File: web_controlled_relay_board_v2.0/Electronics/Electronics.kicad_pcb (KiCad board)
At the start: 2 copper layers, 67 parts, among them J3 Screw_Terminal_01x02, J4 Screw_Terminal_01x02, K1 G3MB-202P, K10 G3MB-202P, K11 G3MB-202P, K12 G3MB-202P, K13 G3MB-202P, K14 G3MB-202P, K15 G3MB-202P, K16 G3MB-202P, K17 G3MB-202P, K18 G3MB-202P, K19 G3MB-202P, K2 G3MB-202P, K20 G3MB-202P, K3 G3MB-202P, K4 G3MB-202P, K5 G3MB-202P, K6 G3MB-202P, K7 G3MB-202P, K8 G3MB-202P, K9 G3MB-202P, SW1 SW_MEC_5E, U1 PC817, U10 PC817, U11 PC817, U12 PC817, U13 PC817, U14 PC817, U15 PC817, U16 PC817, U17 PC817, U18 PC817, U19 PC817, U2 PC817, U20 PC817, U3 PC817, U4 PC817, U5 PC817, U6 PC817, U7 PC817, U8 PC817, U9 PC817

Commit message: PCB finished, pending final touches
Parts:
- added J1: Screw_Terminal_01x10, TerminalBlock_CUI:TerminalBlock_CUI_TB007-508-10_1x10_P5.08mm_Horizontal, F.Cu at (187.8, 47.4)
- added J2: Screw_Terminal_01x10, TerminalBlock_CUI:TerminalBlock_CUI_TB007-508-10_1x10_P5.08mm_Horizontal, F.Cu at (187.8, 128.3)
- moved J3 156.8 mm to (188.0, 33.0), turned to -90 degrees
- moved K1 149.9 mm to (167.9, 31.8)
- moved K10 149.9 mm to (167.9, 106.4)
- moved K2 149.9 mm to (167.9, 40.1)
- moved K3 149.9 mm to (167.9, 48.4)
- moved K4 149.9 mm to (167.9, 56.7)
- moved K5 149.9 mm to (167.9, 65.0)
- moved K6 149.9 mm to (167.9, 73.3)
- moved K7 149.9 mm to (167.9, 81.6)
- moved K8 149.9 mm to (167.9, 89.8)
- moved K9 149.9 mm to (167.9, 98.1)
- moved A1 135.4 mm to (105.8, 190.6), turned to 180 degrees
- moved R17 135.1 mm to (112.4, 178.6)
- moved R19 135.1 mm to (112.4, 186.7)
- moved R15 135.1 mm to (112.4, 170.5)
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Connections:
- A1 pad 1: Control0 -> Control19
- A1 pad 10: Control7 -> Control12
- A1 pad 11: Control8 -> Control11
- A1 pad 12: Control9 -> Control10
- A1 pad 14: Control10 -> Control9
- A1 pad 15: Control11 -> Control8
- A1 pad 16: Control12 -> Control7
- A1 pad 17: Control13 -> Control6
- A1 pad 19: Control14 -> Control5
- A1 pad 2: Control1 -> Control18
- A1 pad 20: Control15 -> Control4
- A1 pad 21: Control16 -> Control3
- A1 pad 22: Control17 -> Control2
- A1 pad 24: Control18 -> Control1
- A1 pad 25: Control19 -> Control0
- A1 pad 39: unconnected-(A1-VSYS-Pad39) -> Net-(A1-VSYS)
- A1 pad 4: Control2 -> Control17
- A1 pad 5: Control3 -> Control16
- A1 pad 6: Control4 -> Control15
- A1 pad 7: Control5 -> Control14
- A1 pad 9: Control6 -> Control13
- J4 pad 1: NEUT -> AC
- J4 pad 2: AC -> NEUT
- PS2 pad 1: AC -> NEUT
- PS2 pad 2: NEUT -> AC
- PowerPin1 pad 2: unconnected-(PowerPin1-Pin_2-Pad2) -> Net-(A1-VSYS)
- U1 pad 1: Net-(R1-Pad2) -> Net-(R2-Pad2)
- U2 pad 1: Net-(R2-Pad2) -> Net-(R1-Pad2)
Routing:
- net GNDA: track 0.00 -> 305.9 mm
- net GND: track 0.00 -> 295.7 mm
- net +5V: track 0.00 -> 213.8 mm
- net GNDD: track 0.00 -> 183.1 mm
- net +3.3V: track 0.00 -> 102.2 mm
- net NEUT: track 0.00 -> 61.1 mm
- net AC: track 0.00 -> 57.3 mm
- net Net-(K1-Pad4): track 0.00 -> 56.7 mm
- net Control0: track 0.00 -> 55.0 mm
- net Net-(K2-Pad4): track 0.00 -> 54.0 mm
- net Net-(K3-Pad4): track 0.00 -> 51.3 mm
- net Net-(K4-Pad4): track 0.00 -> 48.6 mm
- net Control1: track 0.00 -> 48.3 mm
- net Net-(K5-Pad4): track 0.00 -> 46.0 mm
- net Net-(K6-Pad4): track 0.00 -> 43.3 mm
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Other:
- board outline added: 118.9 x 165.9 mm

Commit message: finished final touches of PCB schematic and layout
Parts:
- added C1: C_Polarized, Capacitor_THT:CP_Radial_D6.3mm_P2.50mm, F.Cu at (66.2, 81.6)
- added C2: C_Polarized, Capacitor_THT:CP_Radial_D8.0mm_P3.50mm, F.Cu at (86.7, 28.8)
- moved SW1 62.9 mm to (30.8, 117.9)
- moved U14 55.7 mm to (75.7, 147.3)
- moved U15 55.7 mm to (75.7, 152.9)
- moved U18 55.7 mm to (75.7, 169.7)
- moved J2 55.7 mm to (132.6, 120.9)
- moved J3 55.7 mm to (132.7, 25.7)
- moved K15 55.7 mm to (112.6, 140.3)
- moved K16 55.7 mm to (112.6, 148.6)
- moved K17 55.7 mm to (112.6, 156.9)
- moved K18 55.7 mm to (112.6, 165.2)
- moved U1 55.7 mm to (75.7, 74.7)
- moved U10 55.7 mm to (75.7, 125.0)
- moved U11 55.7 mm to (75.7, 130.6)
- moved U16 55.7 mm to (75.7, 158.5)
- moved U17 55.7 mm to (75.7, 164.1)
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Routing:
- net GNDA: track 305.9 -> 366.1 mm
- net Net-(A1-RUN): track 10.9 -> 48.5 mm
- net +3.3V: track 102.2 -> 131.6 mm
- net +5V: track 213.8 -> 229.8 mm
- net GND: track 295.7 -> 309.8 mm
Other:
- board size 118.9 x 165.9 mm -> 114.6 x 165.2 mm

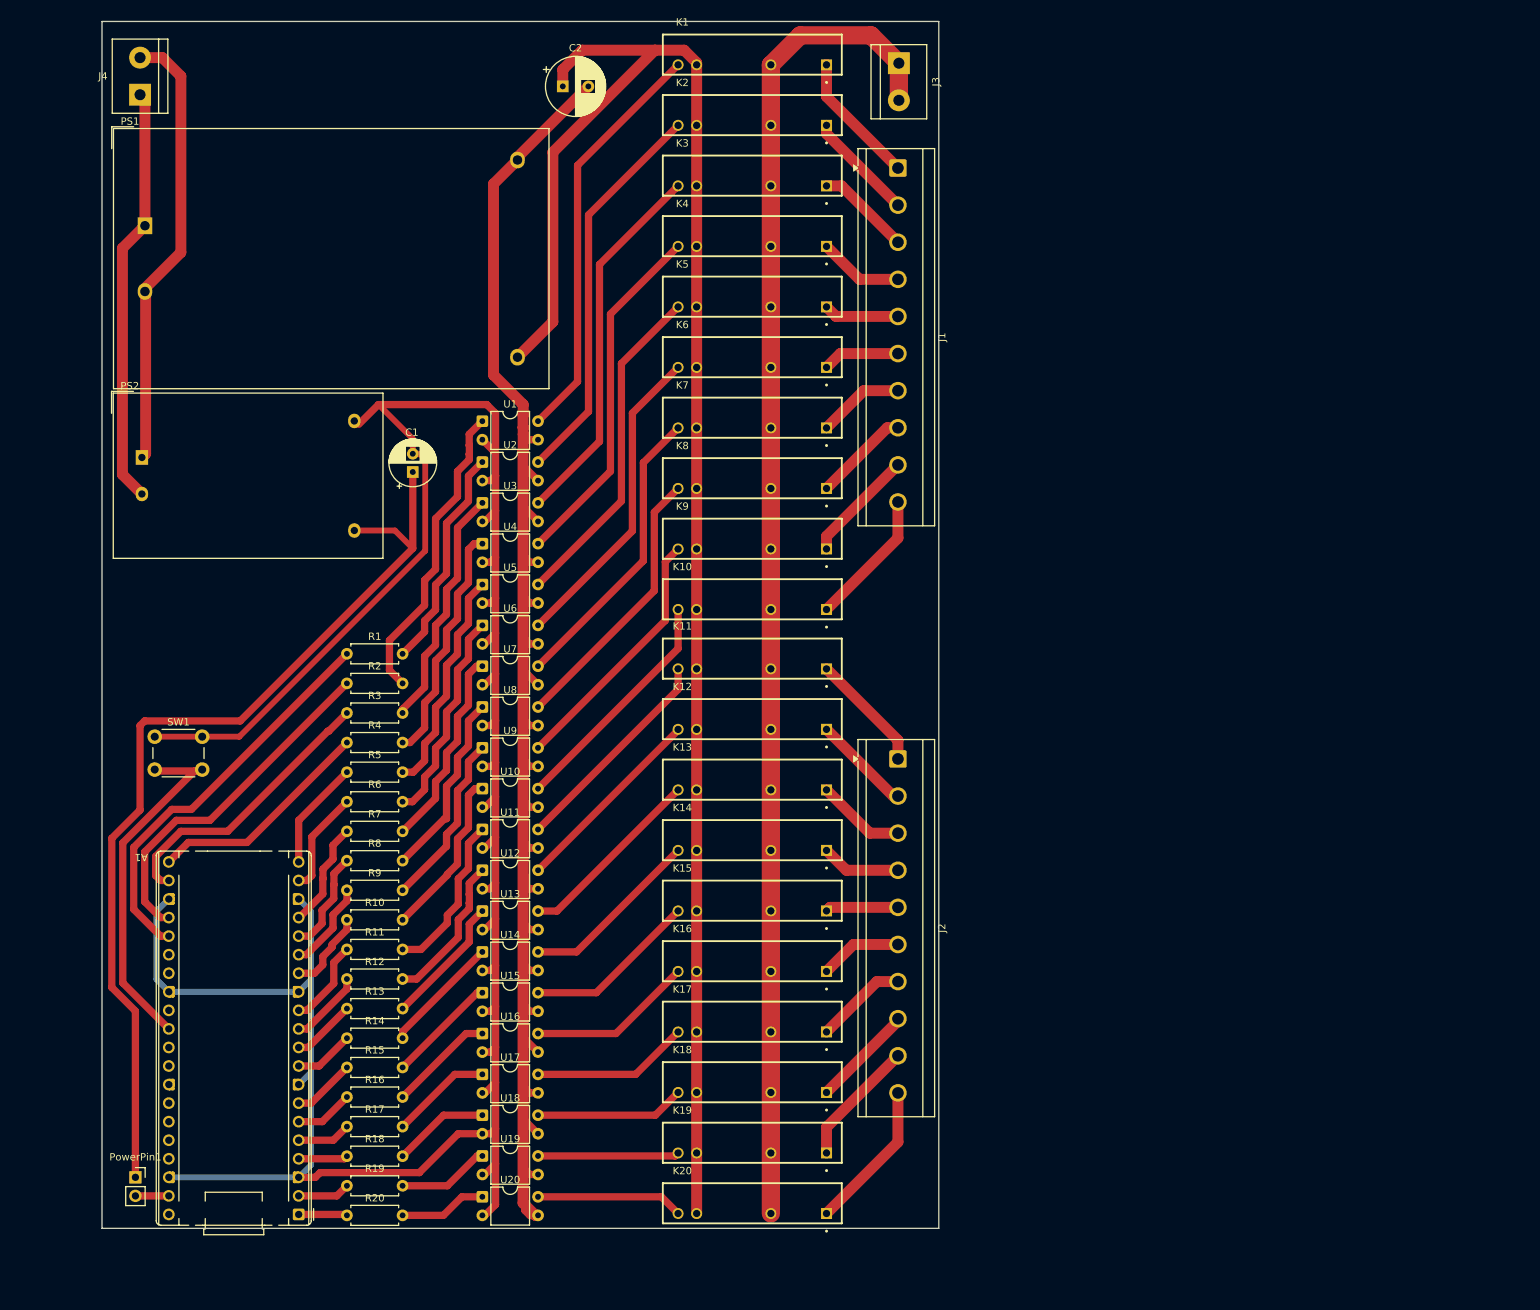
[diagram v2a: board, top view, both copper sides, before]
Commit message: added BOM
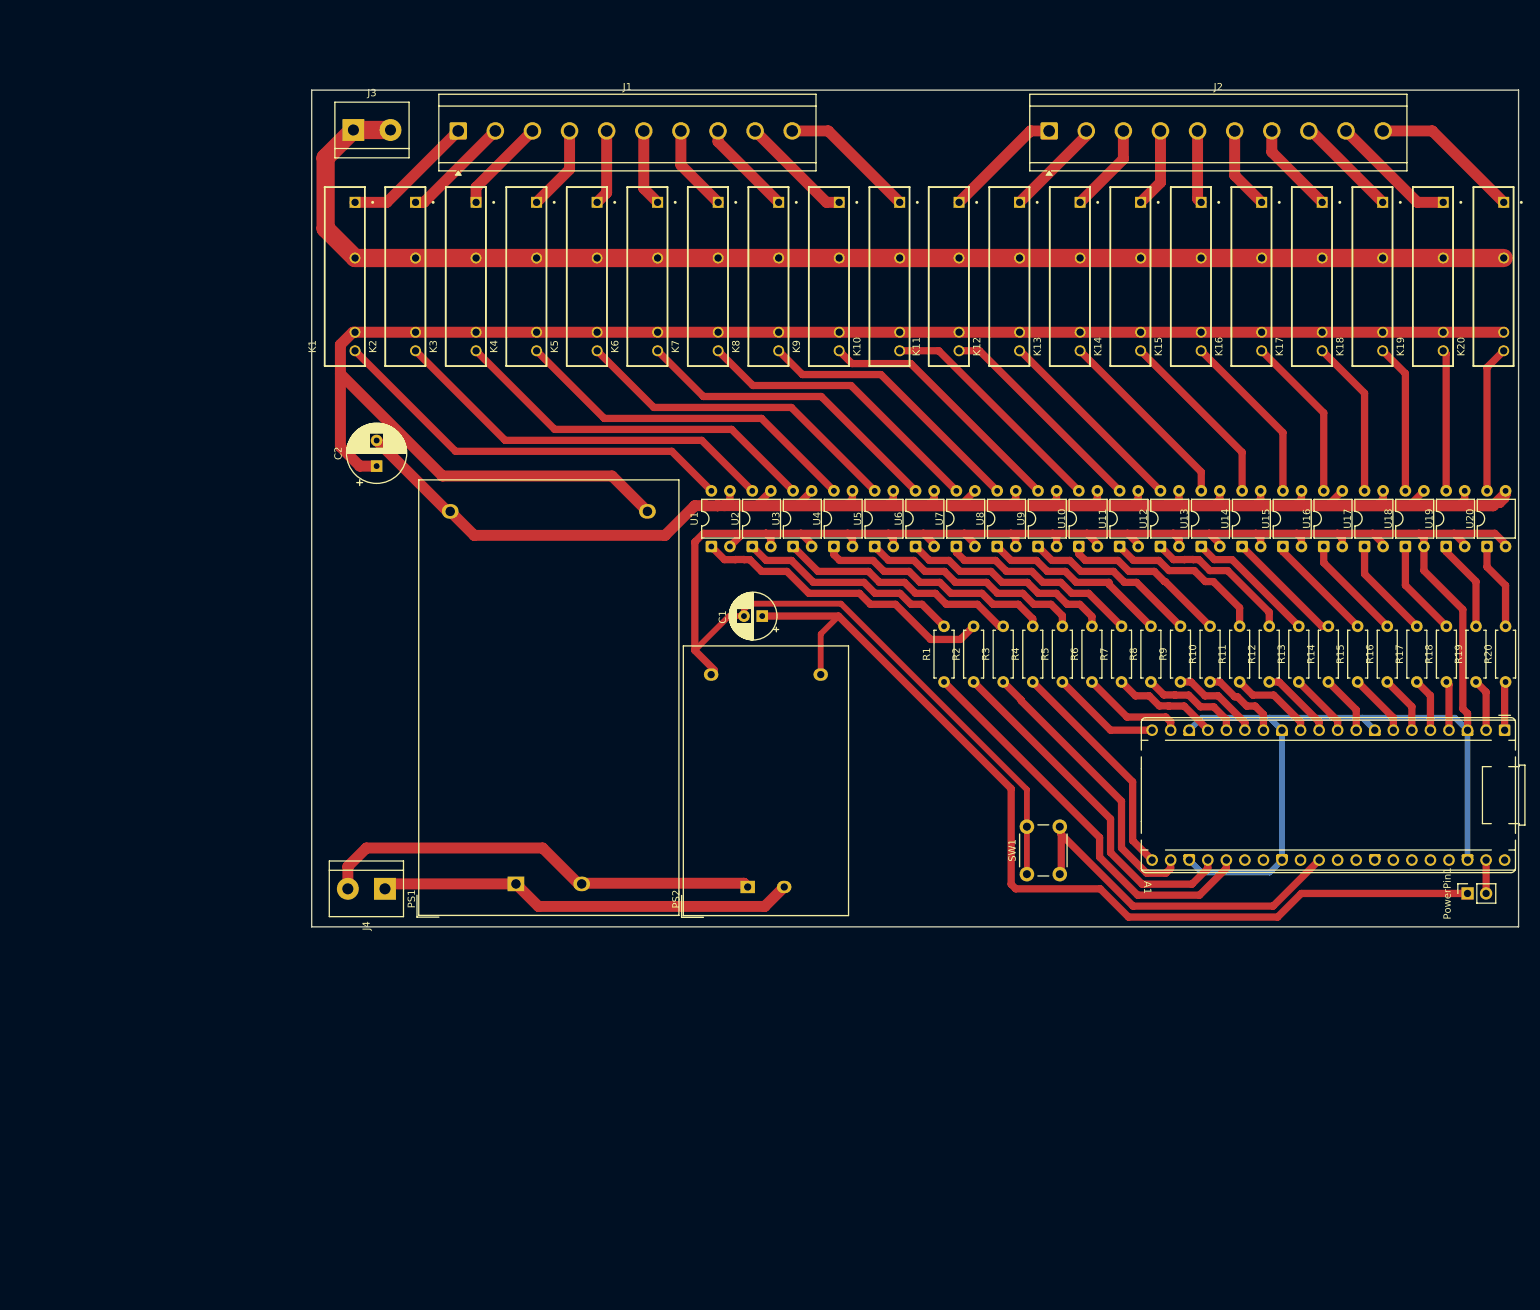
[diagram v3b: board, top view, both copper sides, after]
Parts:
- moved PowerPin1 186.5 mm to (210.6, 139.3), turned to 90 degrees
- moved A1 177.9 mm to (215.6, 117.0), turned to -90 degrees
- moved R20 174.6 mm to (215.8, 110.4), turned to 90 degrees
- moved R19 169.3 mm to (211.7, 110.4), turned to 90 degrees
- moved R18 163.9 mm to (207.7, 110.4), turned to 90 degrees
- moved U20 163.8 mm to (213.2, 91.8), turned to 90 degrees
- moved K20 162.5 mm to (214.1, 54.9), turned to 90 degrees
- moved R17 158.6 mm to (203.6, 110.4), turned to 90 degrees
- moved U19 156.1 mm to (207.6, 91.8), turned to 90 degrees
- moved R16 153.3 mm to (199.6, 110.4), turned to 90 degrees
- moved K19 150.8 mm to (205.8, 54.9), turned to 90 degrees
- moved U18 148.4 mm to (202.1, 91.8), turned to 90 degrees
- moved R15 148.1 mm to (195.5, 110.4), turned to 90 degrees
- moved R14 142.9 mm to (191.5, 110.4), turned to 90 degrees
- moved U17 140.7 mm to (196.5, 91.8), turned to 90 degrees
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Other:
- board size 114.6 x 165.2 mm -> 165.2 x 114.6 mm

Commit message: bug fixes and added docs
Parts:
- moved K16 26.0 mm to (155.1, 58.0)
- moved K17 26.0 mm to (163.4, 58.0)
- moved K18 26.0 mm to (171.7, 58.0)
- moved R11 26.0 mm to (153.5, 113.5)
- moved R13 26.0 mm to (161.6, 113.5)
- moved R16 26.0 mm to (173.7, 113.5)
- moved R19 26.0 mm to (185.9, 113.5)
- moved R6 26.0 mm to (133.3, 113.5)
- moved R8 26.0 mm to (141.4, 113.5)
- moved SW1 26.0 mm to (124.4, 139.8)
- moved U10 26.0 mm to (131.5, 95.0)
- moved U14 26.0 mm to (153.9, 95.0)
- moved U15 26.0 mm to (159.4, 95.0)
- moved C1 26.0 mm to (88.2, 104.5)
- moved K11 26.0 mm to (113.7, 58.0)
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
